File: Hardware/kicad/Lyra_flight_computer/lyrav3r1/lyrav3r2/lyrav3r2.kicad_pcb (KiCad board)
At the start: 4 copper layers, 22 x 52 mm, 110 parts, among them IC1 TESEO-LIV3F, J1 Conn_01x02, J2 Screw_Terminal_01x04, J4 Conn_01x02, J5 Conn_01x05, J6 Screw_Terminal_01x05, J7 USB_B_Micro, Q1 AO3401A, Q2 AO3400A, Q4 AO3400A, Q5 AO3400A, Q6 AO3401A, Q9 AO3400A, U1 E22-900MM22S, U2 BMI088, U3 BMP388, U4 LIS3MDLTR, U5 ADXL375BCCZ-RL7, U6 RT9013-33GB_C19268157, U7 WS7916S-6/TR, U8 RP2040, U9 W25Q128JVS, X2 SX1M12.000M10F30TNN

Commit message: asd
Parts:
- removed the G*** at (190.8, 76.9)
- moved J2 9.85 mm to (206.5, 116.3)
- moved J6 4.75 mm to (186.1, 116.3)
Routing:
- net GND: vias 36 -> 0
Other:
- board size 22 x 52 mm -> 22 x 55 mm
- board text removed: "https://tinyur l.com/mt7vdux4"

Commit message: work, inital layout
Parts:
- removed C15: 120p, Capacitor_SMD:C_0402_1005Metric
- removed D1: D_Schottky, Diode_SMD:D_SOD-323F
- removed Q6: AO3401A, Package_TO_SOT_SMD:SOT-23
- removed U7: WS7916S-6/TR, .pretty:DFN-6_L1.5-W1.0-P0.50-BL
- added C31: 56p, Capacitor_SMD:C_0603_1608Metric, B.Cu at (189.7, 70.7)
- added C35: 56p, Capacitor_SMD:C_0603_1608Metric, B.Cu at (188.2, 70.7)
- added JP1: SolderJumper_3_Open, Jumper:SolderJumper-3_P1.3mm_Open_RoundedPad1.0x1.5mm, B.Cu at (203.2, 81.0)
- added U10: MXDLN16TL, .pretty:LGA-6_L1.1-W0.7-P0.40-BL, B.Cu at (199.2, 84.7)
- BZ1: footprint SamacSys_Parts:CPT1414680T -> Connector_PinHeader_1.27mm:PinHeader_1x02_P1.27mm_Vertical
- L1: value 10n -> 27n
- L4: value 5n6 -> 14n; footprint Inductor_SMD:L_0402_1005Metric -> Inductor_SMD:L_0603_1608Metric
- R20, R21, R22, R23, R24, R25, R26, R27: moved to B.Cu
- moved R22 60.7 mm to (200.8, 117.8), turned to -90 degrees
- moved R23 60.6 mm to (200.8, 119.7), turned to -90 degrees
- moved R20 59.9 mm to (205.7, 115.1), turned to 90 degrees
- moved R21 56.3 mm to (205.7, 113.2), turned to 90 degrees
- moved TP8 49.4 mm to (185.8, 81.7)
- moved R24 49.1 mm to (205.7, 111.3), turned to 90 degrees
- moved TP9 46.2 mm to (187.9, 81.7)
- moved R25 45.6 mm to (205.7, 109.3), turned to 90 degrees
- moved R26 44.8 mm to (200.0, 106.7), turned to 180 degrees
- moved R27 44.4 mm to (198.1, 106.7), turned to 180 degrees
- moved U5 41.3 mm to (193.3, 90.5)
- moved C50 41.3 mm to (196.3, 89.0)
- moved C32 41.2 mm to (196.3, 92.1)
- moved R13 39.6 mm to (191.2, 87.1), turned to -90 degrees
- moved R16 37.9 mm to (192.8, 86.6), turned to 0 degrees
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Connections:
- J2 pad 3: /BATT POSTSW -> /BATT RAW
- J2 pad 4: /BATT RAW -> /BATT POSTSW
- J7 pad 1: VBUS -> unconnected-(J7-VBUS-Pad1)
- L4 pad 1: Net-(C15-Pad2) -> /ANT IN
- Q1 pad 3: Net-(D1-K) -> /BATT POSTSW
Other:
- board size 22 x 55 mm -> 22 x 53 mm
- board text added: "LYRA V3 R2"
- board text removed: "LYRA V3 R1"

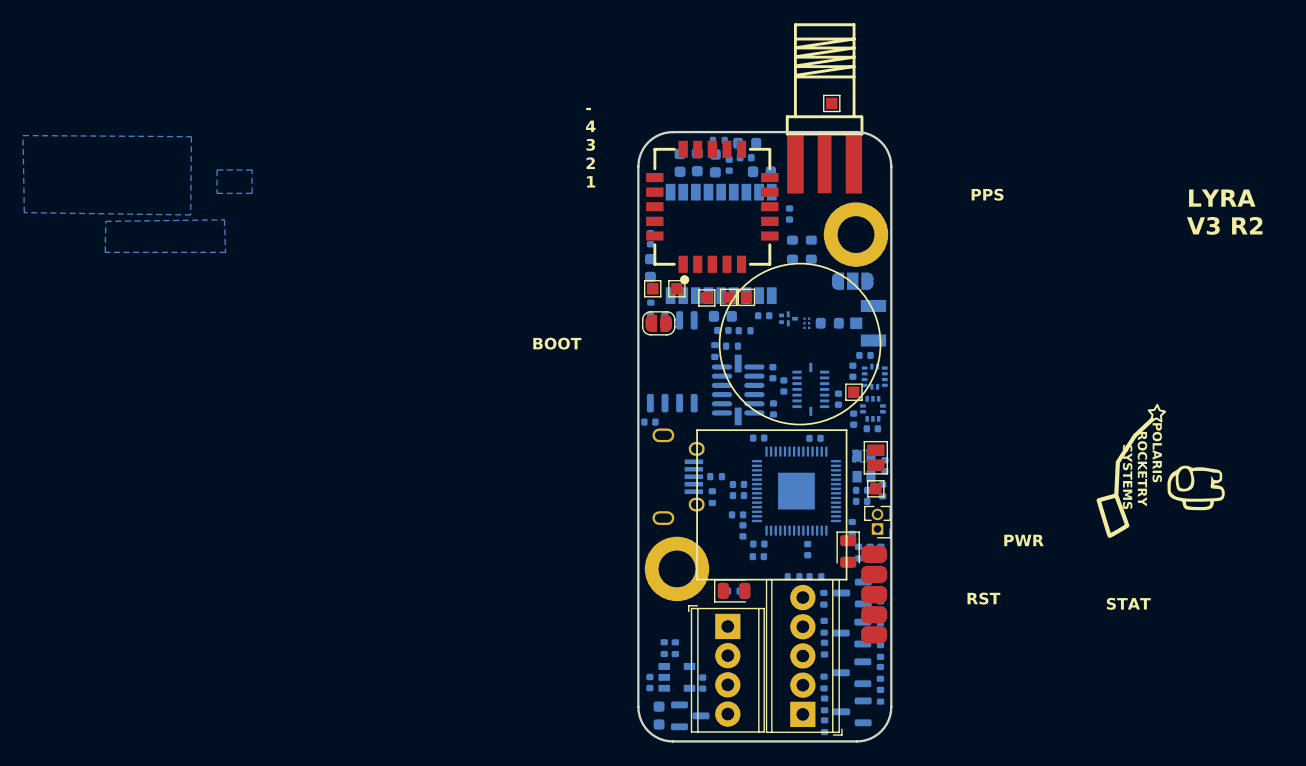
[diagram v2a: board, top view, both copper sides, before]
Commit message: first pass at routing
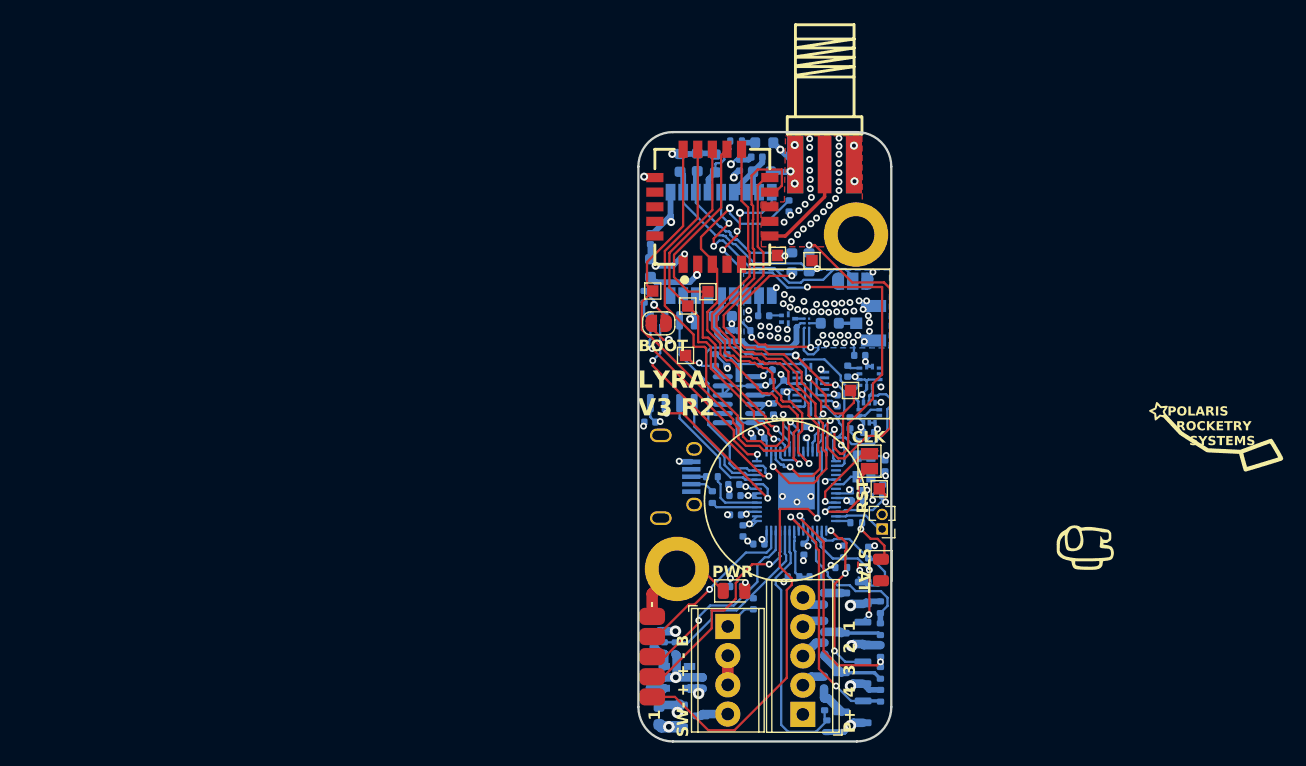
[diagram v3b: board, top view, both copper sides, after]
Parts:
- moved J5 26.0 mm to (185.8, 119.7), turned to 0 degrees
- moved TP3 25.3 mm to (188.7, 87.5)
- moved TP8 14.1 mm to (199.7, 79.2)
- moved G*** 11.0 mm to (225.1, 104.4)
- moved G*** 9.84 mm to (234.7, 97.1), turned to 10 degrees
- moved TP9 9.22 mm to (196.7, 78.8)
- moved TP5 4.74 mm to (185.8, 81.8)
- moved C3 4.12 mm to (194.6, 109.0), turned to -90 degrees
- moved R11 3.68 mm to (202.2, 105.9), turned to 0 degrees
- moved TP7 3.63 mm to (188.9, 83.2)
- moved TP6 3.39 mm to (190.7, 81.9)
- moved D3 3.27 mm to (205.7, 106.1)
- moved R10 2.30 mm to (202.4, 104.5)
- moved R29 1.50 mm to (193.1, 68.8)
- moved D4 1.49 mm to (195.6, 69.0)
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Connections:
- U8 pad 29: /P1 CONT  -> /P3 EN 
- U8 pad 31: /P2 CONT  -> /P2 EN 
- U8 pad 32: /P2 EN  -> /P2 CONT 
- U8 pad 35: /P3 EN  -> /P4 EN 
- U8 pad 36: /P4 CONT  -> /P1 CONT 
- U8 pad 37: /P4 EN  -> /P4 CONT 
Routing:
- net GND: track 0.00 -> 103.0 mm, vias 0 -> 119
- net +3V3: track 0.00 -> 56.6 mm, vias 0 -> 25
- net /GPS_RST: track 0.00 -> 44.1 mm, vias 0 -> 5
- net /TXEN: track 0.00 -> 43.4 mm, vias 0 -> 1
- net /SCK: track 0.00 -> 40.6 mm, vias 0 -> 1
- net /RXEN: track 0.00 -> 40.2 mm, vias 0 -> 1
- net /BRKOUT1: track 0.00 -> 39.6 mm, vias 0 -> 1
- net /SX CS: track 0.00 -> 39.4 mm, vias 0 -> 1
- net /SDA: track 0.00 -> 39.3 mm, vias 0 -> 3
- net /SX RST: track 0.00 -> 38.2 mm, vias 0 -> 2
- net /BUSY: track 0.00 -> 35.7 mm, vias 0 -> 1
- net /SCL: track 0.00 -> 34.5 mm, vias 0 -> 2
- net /MISO: track 0.00 -> 34.1 mm, vias 0 -> 1
- net /MCURX: track 0.00 -> 34.0 mm, vias 0 -> 2
- net /MOSI: track 0.00 -> 32.8 mm, vias 0 -> 1
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- added copper zone on F.Cu, net GND
- removed copper zone on B.Cu, net +3V3
- removed copper zone on B.Cu, net +BATT
- removed copper zone on B.Cu, net /GPS 3v3
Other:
- board text added: "-"
- board text added: "1"
- board text added: "P+ 4 3 2 1"
- board text added: "SW- + + - B"
- board text removed: "- 4 3 2 1"

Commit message: wokrs
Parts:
- moved TP6 1.50 mm to (189.2, 81.5)
- moved AE2 0.28 mm to (204.0, 84.7)
- moved TP7 0.25 mm to (189.2, 83.1)
- moved C9 0.16 mm to (204.0, 87.5)
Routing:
- net GND: track 103.0 -> 100.9 mm, vias 119 -> 110
- net /GPS_RST: track 44.1 -> 42.1 mm, vias 5 -> 4
- net /TXEN: track 43.4 -> 44.7 mm
- net /MISO: track 34.1 -> 33.0 mm
- net /BUSY: track 35.7 -> 36.8 mm
- net /RXEN: track 40.2 -> 41.2 mm
- net /SCK: track 40.6 -> 39.7 mm
- net /SX RST: track 38.2 -> 37.4 mm
- net /ANT OFF: track 11.5 -> 12.1 mm
- net /SX CS: track 39.4 -> 38.8 mm
- added copper zone on In1.Cu, net GND

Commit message: EOD 6/24
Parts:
- added D1: D_Schottky, Diode_SMD:D_SOD-323F, B.Cu at (191.8, 103.6)
- added Q3: AO3401A, Package_TO_SOT_SMD:SOT-23, B.Cu at (188.4, 119.0)
- G***: moved to B.Cu
- moved G*** 45.1 mm to (189.6, 98.1), turned to 90 degrees
- moved G*** 41.5 mm to (193.4, 77.5), turned to -90 degrees
- moved Q1 6.42 mm to (195.5, 117.8), turned to 180 degrees
- moved TP9 1.17 mm to (197.9, 78.7)
- moved C7 0.77 mm to (185.7, 118.4)
- moved R23 0.06 mm to (200.9, 119.7)
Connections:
- J7 pad 1: unconnected-(J7-VBUS-Pad1) -> VBUS
- Q1 pad 1: GND -> VBUS
- Q1 pad 2: +BATT -> Net-(D1-K)
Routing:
- net VBUS: track 0.00 -> 26.2 mm, vias 0 -> 2
- net Net-(D1-K): track 0.00 -> 25.8 mm, vias 0 -> 3
- net /MCUTX: track 23.5 -> 29.7 mm
- net /GPS_RST: track 42.1 -> 45.5 mm
- net /TXEN: track 44.7 -> 42.6 mm, vias 1 -> 3
- net /BUSY: track 36.8 -> 34.8 mm, vias 1 -> 3
- net /RXEN: track 41.2 -> 39.8 mm, vias 1 -> 3
- net /GPSWKUP: track 20.5 -> 21.5 mm
- net +3V3: track 56.6 -> 55.8 mm
- net /GPSTX: track 17.0 -> 17.8 mm
- net /BRKOUT1: track 39.4 -> 40.1 mm
- net GND: track 100.9 -> 100.3 mm, vias 110 -> 116
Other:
- board text removed: "POLARIS ROCKETRY SYSTEMS"
